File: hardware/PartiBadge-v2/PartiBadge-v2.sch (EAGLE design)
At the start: 28 parts, among them J1 I2C, J2 Supply

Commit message: revisions to brd v2
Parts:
- added IC1: (no value), v-reg:78XXS
- renumbered U$4 to PHOTON
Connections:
- removed net 3V3: C1.1, J2.2, PHOTON.3V3, R10.2, R8.2, R9.2, SI7021.VDD, SJ1.2, U$2.PLUS, U$5.VCC
- new net +3V3: C1.1, IC1.OUT, J2.2, PHOTON.VIN, R10.2, R8.2, R9.2, SI7021.VDD, SJ1.2, U$5.VCC
- new net N$5: IC1.IN, U$2.PLUS
- net GND: now also IC1.GND
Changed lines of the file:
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@@
 </part>
 <part name="R8" library="rcl" library_urn="urn:adsk.eagle:library:334" deviceset="R-US_" device="M0805" package3d_urn="urn:adsk.eagle:package:23556/1" value="100"/>
-<part name="U$4" library="Particle-Devices" deviceset="PHOTON" device="_WITH_HEADERS"/>
+<part name="PHOTON" library="Particle-Devices" deviceset="PHOTON" device="_WITH_HEADERS"/>
 <part name="U$5" library="tft_1.8_1.44_oled_0.96" deviceset="OLED_0.96_I2C" device=""/>
 <part name="3V3" library="supply1" library_urn="urn:adsk.eagle:library:371" deviceset="+3V3" device=""/>
@@
 <part name="GND11" library="supply1" library_urn="urn:adsk.eagle:library:371" deviceset="GND" device=""/>
 <part name="U$2" library="SMT18650" deviceset="SMT18650" device=""/>
+<part name="IC1" library="v-reg" library_urn="urn:adsk.eagle:library:409" deviceset="78XXS" device="" package3d_urn="urn:adsk.eagle:package:30342/1"/>
+<part name="GND9" library="supply1" library_urn="urn:adsk.eagle:library:371" deviceset="GND" device=""/>
 </parts>
 <sheets>
@@
 <instance part="PARTIFRAME" gate="V" x="86.36" y="-40.64"/>
 <instance part="R8" gate="G$1" x="86.36" y="48.26" rot="R90"/>
-<instance part="U$4" gate="G$1" x="35.56" y="58.42"/>
+<instance part="PHOTON" gate="G$1" x="35.56" y="58.42"/>
 <instance part="U$5" gate="G$1" x="-15.24" y="111.76" rot="R270"/>
 <instance part="3V3" gate="G$1" x="-38.1" y="124.46"/>
 <instance part="GND5" gate="1" x="-38.1" y="106.68"/>
 <instance part="GND7" gate="1" x="10.16" y="81.28" rot="R270"/>
-<instance part="+3V3" gate="G$1" x="66.04" y="91.44"/>
+<instance part="+3V3" gate="G$1" x="10.16" y="93.98"/>
 <instance part="TSMP58000" gate="G$1" x="40.64" y="-20.32" smashed="yes">
 <attribute name="NAME" x="27.94" y="-15.24" size="1.778" layer="95"/>
@@
 <instance part="C2" gate="G$1" x="50.8" y="-20.32"/>
 <instance part="+3V5" gate="G$1" x="78.74" y="-5.08"/>
-<instance part="+3V8" gate="G$1" x="25.4" y="121.92"/>
+<instance part="+3V8" gate="G$1" x="7.62" y="129.54"/>
 <instance part="GND10" gate="1" x="48.26" y="104.14"/>
 <instance part="GND11" gate="1" x="78.74" y="43.18" rot="R90"/>
 <instance part="U$2" gate="G$1" x="30.48" y="119.38" smashed="yes" rot="R180"/>
+<instance part="IC1" gate="1" x="20.32" y="124.46" rot="R180"/>
+<instance part="GND9" gate="1" x="35.56" y="127"/>
 </instances>
 <busses>
@@
 </segment>
 <segment>
-<pinref part="U$4" gate="G$1" pin="GND@2"/>
+<pinref part="PHOTON" gate="G$1" pin="GND@2"/>
 <wire x1="17.78" y1="81.28" x2="12.7" y2="81.28" width="0.1524" layer="91"/>
 <pinref part="GND7" gate="1" pin="GND"/>
@@
 <wire x1="48.26" y1="114.3" x2="48.26" y2="106.68" width="0.1524" layer="91"/>
 </segment>
-</net>
-<net name="3V3" class="0">
+<segment>
+<pinref part="IC1" gate="1" pin="GND"/>
+<pinref part="GND9" gate="1" pin="GND"/>
+<wire x1="20.32" y1="132.08" x2="35.56" y2="132.08" width="0.1524" layer="91"/>
+<wire x1="35.56" y1="132.08" x2="35.56" y2="129.54" width="0.1524" layer="91"/>
+</segment>
+</net>
+<net name="+3V3" class="0">
 <segment>
 <pinref part="+3V1" gate="G$1" pin="+3V3"/>
@@
 </segment>
 <segment>
-<pinref part="U$4" gate="G$1" pin="3V3"/>
-<wire x1="53.34" y1="86.36" x2="66.04" y2="86.36" width="0.1524" layer="91"/>
+<pinref part="PHOTON" gate="G$1" pin="VIN"/>
 <pinref part="+3V3" gate="G$1" pin="+3V3"/>
-<wire x1="66.04" y1="86.36" x2="66.04" y2="88.9" width="0.1524" layer="91"/>
-</segment>
-<segment>
-<pinref part="U$2" gate="G$1" pin="PLUS"/>
-<wire x1="30.48" y1="114.3" x2="25.4" y2="114.3" width="0.1524" layer="91"/>
+<wire x1="17.78" y1="86.36" x2="10.16" y2="86.36" width="0.1524" layer="91"/>
+<wire x1="10.16" y1="86.36" x2="10.16" y2="91.44" width="0.1524" layer="91"/>
+</segment>
+<segment>
 <pinref part="+3V8" gate="G$1" pin="+3V3"/>
-<wire x1="25.4" y1="114.3" x2="25.4" y2="119.38" width="0.1524" layer="91"/>
+<wire x1="7.62" y1="127" x2="7.62" y2="124.46" width="0.1524" layer="91"/>
+<pinref part="IC1" gate="1" pin="OUT"/>
+<wire x1="7.62" y1="124.46" x2="12.7" y2="124.46" width="0.1524" layer="91"/>
 </segment>
 </net>
@@
 </segment>
 <segment>
-<pinref part="U$4" gate="G$1" pin="RX"/>
+<pinref part="PHOTON" gate="G$1" pin="RX"/>
 <wire x1="17.78" y1="71.12" x2="0" y2="71.12" width="0.1524" layer="91"/>
 <label x="0" y="71.12" size="1.778" layer="95"/>
@@
 </segment>
 <segment>
-<pinref part="U$4" gate="G$1" pin="A4"/>
+<pinref part="PHOTON" gate="G$1" pin="A4"/>
 <wire x1="17.78" y1="50.8" x2="0" y2="50.8" width="0.1524" layer="91"/>
 <label x="0" y="50.8" size="1.778" layer="95"/>
@@
 </segment>
 <segment>
-<pinref part="U$4" gate="G$1" pin="A3"/>
+<pinref part="PHOTON" gate="G$1" pin="A3"/>
 <wire x1="17.78" y1="45.72" x2="0" y2="45.72" width="0.1524" layer="91"/>
 <label x="0" y="45.72" size="1.778" layer="95"/>
@@
 </segment>
 <segment>
-<pinref part="U$4" gate="G$1" pin="A2"/>
+<pinref part="PHOTON" gate="G$1" pin="A2"/>
 <wire x1="17.78" y1="40.64" x2="0" y2="40.64" width="0.1524" layer="91"/>
 <label x="0" y="40.64" size="1.778" layer="95"/>
@@
 </segment>
 <segment>
-<pinref part="U$4" gate="G$1" pin="A1"/>
+<pinref part="PHOTON" gate="G$1" pin="A1"/>
 <wire x1="17.78" y1="35.56" x2="0" y2="35.56" width="0.1524" layer="91"/>
 <label x="0" y="35.56" size="1.778" layer="95"/>
@@
 </segment>
 <segment>
-<pinref part="U$4" gate="G$1" pin="A5"/>
+<pinref part="PHOTON" gate="G$1" pin="A5"/>
 <wire x1="17.78" y1="55.88" x2="0" y2="55.88" width="0.1524" layer="91"/>
 <label x="0" y="55.88" size="1.778" layer="95"/>
@@
 </segment>
 <segment>
-<pinref part="U$4" gate="G$1" pin="D0"/>
+<pinref part="PHOTON" gate="G$1" pin="D0"/>
 <wire x1="53.34" y1="30.48" x2="58.42" y2="30.48" width="0.1524" layer="91"/>
 <label x="53.34" y="30.48" size="1.778" layer="95"/>
@@
 </segment>
 <segment>
-<pinref part="U$4" gate="G$1" pin="D1"/>
+<pinref part="PHOTON" gate="G$1" pin="D1"/>
 <wire x1="53.34" y1="35.56" x2="58.42" y2="35.56" width="0.1524" layer="91"/>
 <label x="53.34" y="35.56" size="1.778" layer="95"/>
@@
 </segment>
 <segment>
-<pinref part="U$4" gate="G$1" pin="D7"/>
+<pinref part="PHOTON" gate="G$1" pin="D7"/>
 <wire x1="53.34" y1="66.04" x2="63.5" y2="66.04" width="0.1524" layer="91"/>
 <label x="60.96" y="66.04" size="1.778" layer="95"/>
@@
 </segment>
 <segment>
-<pinref part="U$4" gate="G$1" pin="D6"/>
+<pinref part="PHOTON" gate="G$1" pin="D6"/>
 <wire x1="53.34" y1="60.96" x2="63.5" y2="60.96" width="0.1524" layer="91"/>
 <label x="56.642" y="60.96" size="1.778" layer="95"/>
@@
 </segment>
 <segment>
-<pinref part="U$4" gate="G$1" pin="D5"/>
+<pinref part="PHOTON" gate="G$1" pin="D5"/>
 <wire x1="53.34" y1="55.88" x2="63.5" y2="55.88" width="0.1524" layer="91"/>
 <label x="58.42" y="55.88" size="1.778" layer="95"/>
@@
 </segment>
 <segment>
-<pinref part="U$4" gate="G$1" pin="D4"/>
+<pinref part="PHOTON" gate="G$1" pin="D4"/>
 <wire x1="53.34" y1="50.8" x2="63.5" y2="50.8" width="0.1524" layer="91"/>
 <label x="56.896" y="51.054" size="1.778" layer="95"/>
@@
 </segment>
 <segment>
-<pinref part="U$4" gate="G$1" pin="D3"/>
+<pinref part="PHOTON" gate="G$1" pin="D3"/>
 <wire x1="53.34" y1="45.72" x2="63.5" y2="45.72" width="0.1524" layer="91"/>
 <label x="58.42" y="45.72" size="1.778" layer="95"/>
@@
 <segment>
 <pinref part="R7" gate="G$1" pin="2"/>
-<pinref part="U$4" gate="G$1" pin="TX"/>
+<pinref part="PHOTON" gate="G$1" pin="TX"/>
 <wire x1="-2.54" y1="76.2" x2="17.78" y2="76.2" width="0.1524" layer="91"/>
 </segment>
@@
 </segment>
 <segment>
-<pinref part="U$4" gate="G$1" pin="A0"/>
+<pinref part="PHOTON" gate="G$1" pin="A0"/>
 <wire x1="17.78" y1="30.48" x2="0" y2="30.48" width="0.1524" layer="91"/>
 <label x="0" y="30.48" size="1.778" layer="95"/>
@@
 </segment>
 <segment>
-<pinref part="U$4" gate="G$1" pin="WKP"/>
+<pinref part="PHOTON" gate="G$1" pin="WKP"/>
 <wire x1="17.78" y1="66.04" x2="0" y2="66.04" width="0.1524" layer="91"/>
 <label x="0" y="66.04" size="1.778" layer="95"/>
@@
 </segment>
 <segment>
-<pinref part="U$4" gate="G$1" pin="DAC"/>
+<pinref part="PHOTON" gate="G$1" pin="DAC"/>
 <wire x1="17.78" y1="60.96" x2="0" y2="60.96" width="0.1524" layer="91"/>
 <label x="0" y="60.96" size="1.778" layer="95"/>
@@
 <net name="N$2" class="0">
 <segment>
-<pinref part="U$4" gate="G$1" pin="D2"/>
+<pinref part="PHOTON" gate="G$1" pin="D2"/>
 <pinref part="S5" gate="1" pin="P"/>
 <wire x1="53.34" y1="40.64" x2="66.04" y2="40.64" width="0.1524" layer="91"/>
@@
 </segment>
 </net>
+<net name="N$5" class="0">
+<segment>
+<pinref part="U$2" gate="G$1" pin="PLUS"/>
+<pinref part="IC1" gate="1" pin="IN"/>
+<wire x1="30.48" y1="114.3" x2="27.94" y2="114.3" width="0.1524" layer="91"/>
+<wire x1="27.94" y1="114.3" x2="27.94" y2="124.46" width="0.1524" layer="91"/>
+</segment>
+</net>

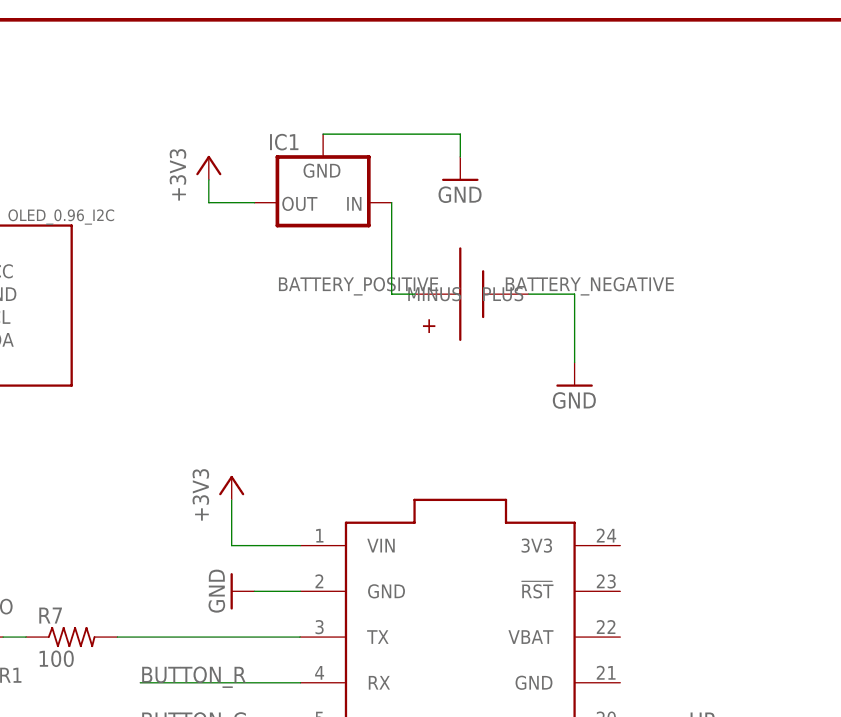
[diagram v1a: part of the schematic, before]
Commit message: fixed power routing and made 3V3 traces wider
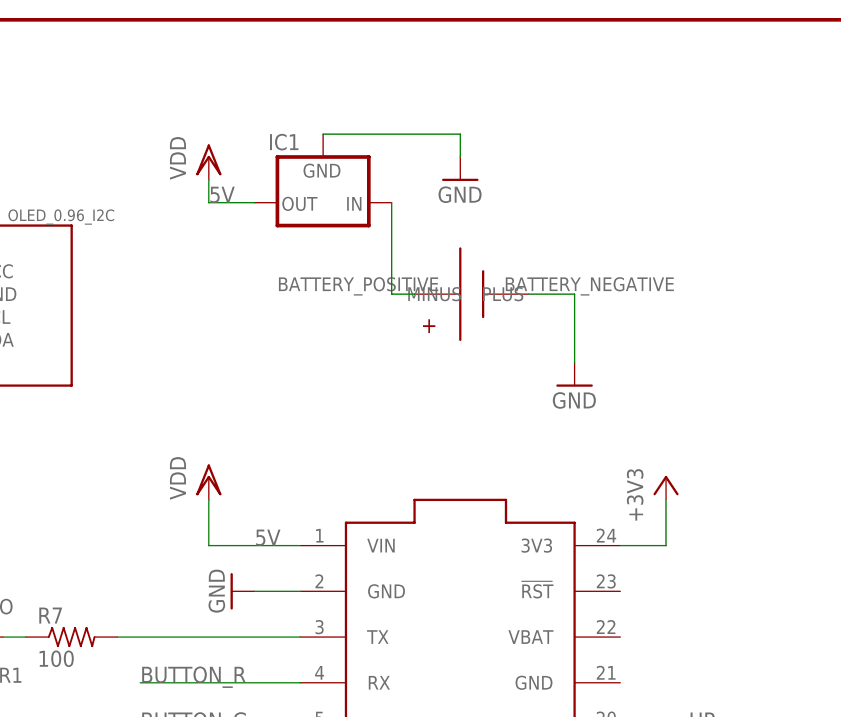
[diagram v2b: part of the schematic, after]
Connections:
- new net 5V: IC1.OUT, PHOTON.VIN
- net +3V3: now also PHOTON.3V3; no longer IC1.OUT, PHOTON.VIN
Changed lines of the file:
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@@
 <part name="GND5" library="supply1" library_urn="urn:adsk.eagle:library:371" deviceset="GND" device=""/>
 <part name="GND7" library="supply1" library_urn="urn:adsk.eagle:library:371" deviceset="GND" device=""/>
-<part name="+3V3" library="supply1" library_urn="urn:adsk.eagle:library:371" deviceset="+3V3" device=""/>
 <part name="TSMP58000" library="transistor-npn" library_urn="urn:adsk.eagle:library:398" deviceset="2N3704" device="" package3d_urn="urn:adsk.eagle:package:28974/2" value="IR Sensor"/>
 <part name="GND8" library="supply1" library_urn="urn:adsk.eagle:library:371" deviceset="GND" device=""/>
@@
 <part name="C2" library="SparkFun-Capacitors" library_urn="urn:adsk.eagle:library:510" deviceset="0.1UF" device="-0603-25V-(+80/-20%)" package3d_urn="urn:adsk.eagle:package:37414/1" value="4.7uF"/>
 <part name="+3V5" library="supply1" library_urn="urn:adsk.eagle:library:371" deviceset="+3V3" device=""/>
-<part name="+3V8" library="supply1" library_urn="urn:adsk.eagle:library:371" deviceset="+3V3" device=""/>
 <part name="GND10" library="supply1" library_urn="urn:adsk.eagle:library:371" deviceset="GND" device=""/>
 <part name="GND11" library="supply1" library_urn="urn:adsk.eagle:library:371" deviceset="GND" device=""/>
@@
 <part name="IC1" library="v-reg" library_urn="urn:adsk.eagle:library:409" deviceset="78XXS" device="" package3d_urn="urn:adsk.eagle:package:30342/1"/>
 <part name="GND9" library="supply1" library_urn="urn:adsk.eagle:library:371" deviceset="GND" device=""/>
+<part name="+3V7" library="supply1" library_urn="urn:adsk.eagle:library:371" deviceset="+3V3" device=""/>
+<part name="VDD1" library="supply1" library_urn="urn:adsk.eagle:library:371" deviceset="VDD" device=""/>
+<part name="VDD2" library="supply1" library_urn="urn:adsk.eagle:library:371" deviceset="VDD" device=""/>
 </parts>
 <sheets>
@@
 <instance part="GND5" gate="1" x="-38.1" y="106.68"/>
 <instance part="GND7" gate="1" x="10.16" y="81.28" rot="R270"/>
-<instance part="+3V3" gate="G$1" x="10.16" y="93.98"/>
 <instance part="TSMP58000" gate="G$1" x="40.64" y="-20.32" smashed="yes">
 <attribute name="NAME" x="27.94" y="-15.24" size="1.778" layer="95"/>
@@
 <instance part="C2" gate="G$1" x="50.8" y="-20.32"/>
 <instance part="+3V5" gate="G$1" x="78.74" y="-5.08"/>
-<instance part="+3V8" gate="G$1" x="7.62" y="129.54"/>
 <instance part="GND10" gate="1" x="48.26" y="104.14"/>
 <instance part="GND11" gate="1" x="78.74" y="43.18" rot="R90"/>
@@
 <instance part="IC1" gate="1" x="20.32" y="124.46" rot="R180"/>
 <instance part="GND9" gate="1" x="35.56" y="127"/>
+<instance part="+3V7" gate="G$1" x="58.42" y="93.98"/>
+<instance part="VDD1" gate="G$1" x="7.62" y="93.98"/>
+<instance part="VDD2" gate="G$1" x="7.62" y="129.54"/>
 </instances>
 <busses>
@@
 </segment>
 <segment>
-<pinref part="PHOTON" gate="G$1" pin="VIN"/>
-<pinref part="+3V3" gate="G$1" pin="+3V3"/>
-<wire x1="17.78" y1="86.36" x2="10.16" y2="86.36" width="0.1524" layer="91"/>
-<wire x1="10.16" y1="86.36" x2="10.16" y2="91.44" width="0.1524" layer="91"/>
-</segment>
-<segment>
-<pinref part="+3V8" gate="G$1" pin="+3V3"/>
-<wire x1="7.62" y1="127" x2="7.62" y2="124.46" width="0.1524" layer="91"/>
-<pinref part="IC1" gate="1" pin="OUT"/>
-<wire x1="7.62" y1="124.46" x2="12.7" y2="124.46" width="0.1524" layer="91"/>
+<pinref part="PHOTON" gate="G$1" pin="3V3"/>
+<wire x1="53.34" y1="86.36" x2="58.42" y2="86.36" width="0.1524" layer="91"/>
+<wire x1="58.42" y1="86.36" x2="58.42" y2="91.44" width="0.1524" layer="91"/>
+<pinref part="+3V7" gate="G$1" pin="+3V3"/>
 </segment>
 </net>
@@
 </segment>
 </net>
+<net name="5V" class="0">
+<segment>
+<pinref part="IC1" gate="1" pin="OUT"/>
+<pinref part="VDD2" gate="G$1" pin="VDD"/>
+<wire x1="12.7" y1="124.46" x2="7.62" y2="124.46" width="0.1524" layer="91"/>
+<wire x1="7.62" y1="124.46" x2="7.62" y2="127" width="0.1524" layer="91"/>
+<label x="7.62" y="124.46" size="1.778" layer="95"/>
+</segment>
+<segment>
+<pinref part="PHOTON" gate="G$1" pin="VIN"/>
+<wire x1="17.78" y1="86.36" x2="7.62" y2="86.36" width="0.1524" layer="91"/>
+<label x="12.7" y="86.36" size="1.778" layer="95"/>
+<pinref part="VDD1" gate="G$1" pin="VDD"/>
+<wire x1="7.62" y1="86.36" x2="7.62" y2="91.44" width="0.1524" layer="91"/>
+</segment>
+</net>

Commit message: widened traces from batt to converter
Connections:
- net N$5 renamed VIN
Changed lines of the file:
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@@
-</segment>
-</net>
-<net name="N$5" class="0">
-<segment>
-<pinref part="U$2" gate="G$1" pin="PLUS"/>
-<pinref part="IC1" gate="1" pin="IN"/>
-<wire x1="30.48" y1="114.3" x2="27.94" y2="114.3" width="0.1524" layer="91"/>
-<wire x1="27.94" y1="114.3" x2="27.94" y2="124.46" width="0.1524" layer="91"/>
 </segment>
 </net>
@@
 </segment>
 </net>
+<net name="VIN" class="0">
+<segment>
+<pinref part="U$2" gate="G$1" pin="PLUS"/>
+<pinref part="IC1" gate="1" pin="IN"/>
+<wire x1="30.48" y1="114.3" x2="27.94" y2="114.3" width="0.1524" layer="91"/>
+<wire x1="27.94" y1="114.3" x2="27.94" y2="124.46" width="0.1524" layer="91"/>
+</segment>
+</net>

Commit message: fix v2 board issues
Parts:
- removed TSMP58000: IR Sensor, transistor-npn:2N3704
- removed U$2: SMT18650, SMT18650:SMT18650
- added IC2: TSMP58000, TSMP58000:TSMP58000
- added U1: 1042, 1042:1042
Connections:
- removed net VIN: IC1.IN, U$2.PLUS
- new net BATT: IC1.IN, U1.POS
- net BUTTON_B: now also PHOTON.A5; no longer PHOTON.DAC
- net BUTTON_G: now also PHOTON.DAC; no longer PHOTON.WKP
- net BUTTON_R: now also PHOTON.WKP; no longer PHOTON.RX
- net BUTTON_Y: now also PHOTON.A4; no longer PHOTON.A5
- net GND: now also IC2.GND, U1.NEG; no longer TSMP58000.E, U$2.MINUS
- net IR_RECEIVER: now also IC2.OUT, PHOTON.RX; no longer PHOTON.A0, TSMP58000.B
- net LED_B: now also PHOTON.A1; no longer PHOTON.A2
- net LED_G: now also PHOTON.A2; no longer PHOTON.A3
- net LED_R: now also PHOTON.A3; no longer PHOTON.A4
- net LED_Y: now also PHOTON.A0; no longer PHOTON.A1
- net N$9: now also IC2.VS; no longer TSMP58000.C
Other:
- moved on the sheet: C2, R10, R9
